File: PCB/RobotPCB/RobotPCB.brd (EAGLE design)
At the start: 50.8 x 50.8 mm, 42 parts, among them IC1 MPU6050, IC2 MCP73831/OT, U1 DRV8835, U2 CP2104-F03-GM

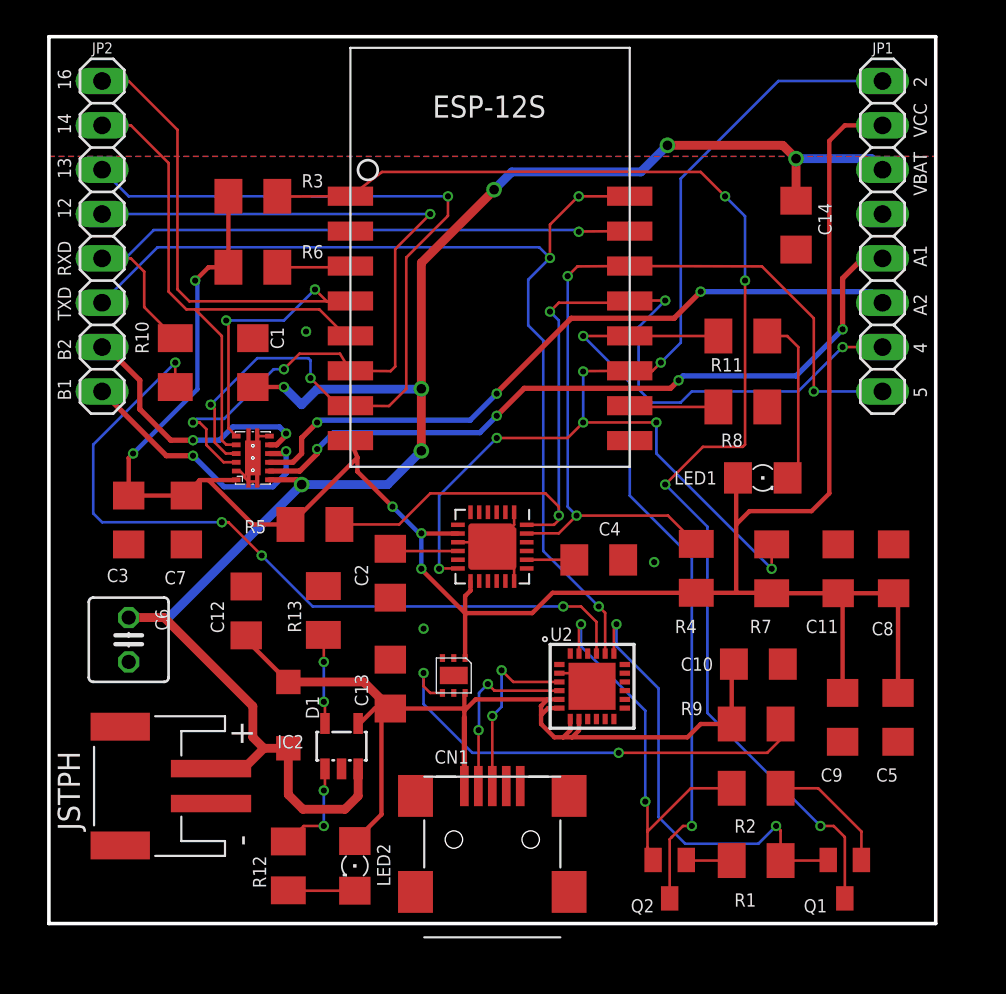
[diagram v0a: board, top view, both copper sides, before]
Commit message: Started some mounting holes
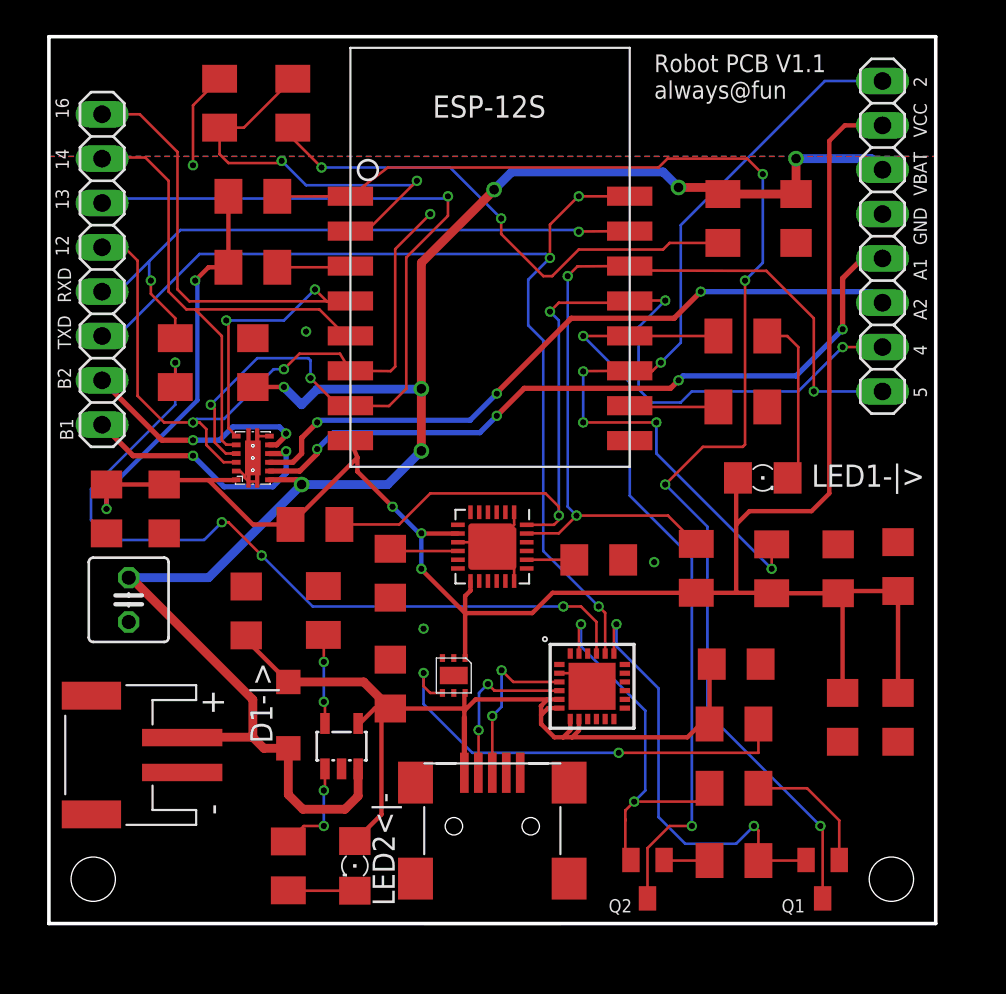
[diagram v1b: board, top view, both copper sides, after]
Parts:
- added R14: 10k, rcl:M1206
- added R15: 3.3k, rcl:M1206
- added R16: 1k, rcl:M1206
- R1: value 10ki -> 10k
- moved JSTPH 2.43 mm to (3.94, 9.65)
- moved C6 2.29 mm to (4.57, 18.5)
- moved JP2 1.90 mm to (3.05, 37.5)
- moved C3 1.42 mm to (3.30, 23.7)
- moved C7 1.42 mm to (6.60, 23.7)
- moved C10 1.27 mm to (39.4, 14.9)
- moved Q1 1.27 mm to (44.3, 2.54)
- moved Q2 1.27 mm to (34.3, 2.54)
- moved R1 1.27 mm to (39.2, 3.61)
- moved R2 1.27 mm to (39.2, 7.75)
- moved R9 1.27 mm to (39.2, 11.4)
- moved CN1 0.76 mm to (25.4, 4.57)
- moved C14 0.38 mm to (42.8, 40.4)
- moved C8 0.28 mm to (48.6, 20.4)
- renumbered D1 to D1-|>, LED1 to LED1-|>, LED2 to LED2<|-
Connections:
- new net N$6: R14.2, R16.1
- net ADC: now also R14.1, R15.2
- net GND: now also R15.1
- net GPIO2: no longer IC1.12
- net VBAT: now also R16.2
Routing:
- net N$6: track 0.00 -> 29.8 mm, vias 0 -> 2
- net ADC: track 0.00 -> 24.1 mm, vias 0 -> 2
- net GPIO2: track 64.4 -> 47.6 mm, vias 7 -> 5
- net GND: track 11.5 -> 17.1 mm, vias 3 -> 4
- net GPIO12: track 46.2 -> 41.3 mm
- net VCC: track 130.3 -> 134.3 mm
- net RESET: track 75.3 -> 77.8 mm
- net VBUS: track 56.4 -> 54.3 mm
- net MOUTB2: track 15.5 -> 13.7 mm
- net GPIO16: track 38.4 -> 36.9 mm
- net RXD: track 38.2 -> 36.8 mm, vias 1 -> 2
- net GPIO14: track 32.6 -> 31.3 mm
- net RTS: track 26.4 -> 25.1 mm
- net USB_RX: track 45.2 -> 46.4 mm
- net GPIO0: track 44.1 -> 45.1 mm
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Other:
- board text added: "GND"
- board text added: "Robot PCB V1.1 always@fun"

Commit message: Optimized Robot PCB
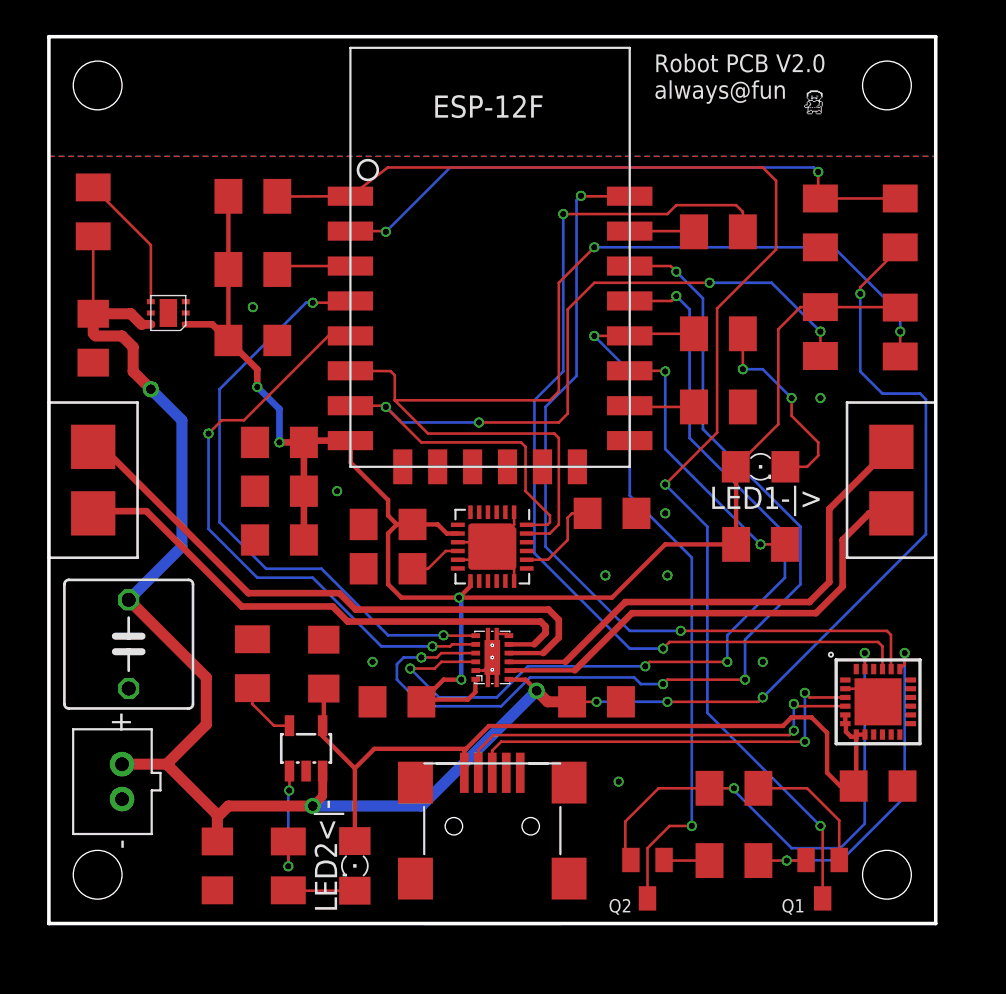
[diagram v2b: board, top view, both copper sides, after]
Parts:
- removed C6: 1.0 uF, rcl:C025-050X050
- removed D1-|>: MBR120HW, diode:SOD123
- removed JP1, JP2: (no value), pinhead:1X08
- removed JSTPH: (no value), adafruit:JST-PH-2-SMT-RA
- removed R16: 1k, rcl:M1206
- added C15: 1 mF, rcl:C050-075X075
- added CN2: (no value), adafruit:JST-PH-2-THM
- added U$3, U$4: MOTOR_PAD, ECE5780-MotorDriver:MOTOR_PAD
- R14: value 10k -> 39k
- R15: value 3.3k -> 10k
- moved C14 49.7 mm to (9.65, 3.30)
- moved R9 47.0 mm to (2.54, 40.8), turned to 90 degrees
- moved C10 41.3 mm to (2.54, 33.5), turned to 270 degrees
- moved C12 37.6 mm to (47.5, 7.87), turned to 0 degrees
- moved C5 36.9 mm to (13.2, 22.0), turned to 180 degrees
- moved C8 36.1 mm to (13.2, 27.6), turned to 180 degrees
- moved C11 36.0 mm to (11.7, 33.4), turned to 0 degrees
- moved R14 35.5 mm to (48.8, 40.1)
- moved R15 35.1 mm to (44.2, 40.1), turned to 90 degrees
- moved C9 34.8 mm to (13.2, 24.8), turned to 180 degrees
- moved R10 32.0 mm to (38.4, 39.6), turned to 180 degrees
- moved R5 31.0 mm to (44.2, 33.9), turned to 90 degrees
- moved C1 27.7 mm to (31.4, 12.7), turned to 0 degrees
- moved U$2 25.2 mm to (7.84, 36.0), turned to 180 degrees
- moved C3 20.0 mm to (19.9, 12.7), turned to 180 degrees
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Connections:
- removed net N$6: R14.2, R16.1
- net GND: now also C15.2, CN2.2; no longer C6.2, JP1.5, JSTPH.2
- net GPIO12: now also IC1.23, R4.1; no longer JP2.4, U1.10
- net GPIO13: now also IC1.24, R5.1; no longer JP2.3, U1.9
- net GPIO14: no longer JP2.2
- net GPIO16: no longer JP2.1
- net GPIO2: no longer JP1.8
- net GPIO4: now also U1.10; no longer IC1.24, JP1.2, R5.1
- net GPIO5: now also U1.9; no longer IC1.23, JP1.1, R4.1
- net MOUTA1: now also U$3.1; no longer JP1.4
- net MOUTA2: now also U$3.2; no longer JP1.3
- net MOUTB1: now also U$4.1; no longer JP2.8
- net MOUTB2: now also U$4.2; no longer JP2.7
- net RXD: no longer JP2.5
- net TXD: no longer JP2.6
- net VBAT: now also C10.1, C15.1, CN2.1, R14.2, R9.1, U$2.6; no longer C6.1, D1-|>.A, JP1.6, JSTPH.1, R16.2
- net VBUS: no longer C10.1, D1-|>.C, R9.1, U$2.6
- net VCC: no longer JP1.7
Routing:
- net VCC: track 134.3 -> 96.3 mm, vias 5 -> 4
- net RXD: track 36.8 -> 3.70 mm, vias 2 -> 0
- net GPIO2: track 47.6 -> 15.6 mm, vias 5 -> 2
- net N$6: track 29.8 -> 0.00 mm, vias 2 -> 0
- net MOUTB1: track 14.6 -> 35.0 mm, vias 2 -> 0
- net GPIO12: track 41.3 -> 61.6 mm, vias 3 -> 2
- net VBAT: track 101.9 -> 121.2 mm
- net N$3: track 25.8 -> 7.91 mm, vias 2 -> 0
- net MOUTB2: track 13.7 -> 31.4 mm, vias 2 -> 0
- net N$4: track 9.67 -> 24.6 mm
- net MOUTA1: track 42.0 -> 27.2 mm, vias 4 -> 0
- net N$7: track 9.56 -> 24.3 mm
- net TXD: track 59.8 -> 47.6 mm, vias 3 -> 2
- net MOUTA2: track 40.0 -> 29.5 mm, vias 3 -> 0
- net ADC: track 24.1 -> 34.6 mm
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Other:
- board text added: "Robot PCB V2.0 always@fun"
- board text removed: "12"
- board text removed: "13"
- board text removed: "14"
- board text removed: "16"
- board text removed: "2"
- board text removed: "4"
- board text removed: "5"
- board text removed: "A1"
- board text removed: "A2"
- board text removed: "B1"
- board text removed: "B2"
- board text removed: "GND"
- board text removed: "RXD"
- board text removed: "Robot PCB V1.1 always@fun"
- board text removed: "TXD"
- board text removed: "VBAT"
- board text removed: "VCC"

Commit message: Fixed PCB mounting holes
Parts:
- R14: value 39k -> 33k
- moved Q1 0.76 mm to (43.6, 2.54)
- moved Q2 0.76 mm to (33.5, 2.54)
- moved R1 0.76 mm to (38.5, 3.61)
- moved R2 0.76 mm to (38.5, 7.75)
- moved CN2 0.36 mm to (4.45, 8.38), turned to 0 degrees
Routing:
- net GPIO0: track 42.1 -> 43.0 mm
- net RTS: track 20.3 -> 21.1 mm
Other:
- board text added: "Robot PCB V2.1 always@fun"
- board text removed: "Robot PCB V2.0 always@fun"

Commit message: Finalized Robot PCB
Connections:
- net GND: now also U1.PAD5, U1.PAD6, U1.PAD7
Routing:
- net GND: track 15.6 -> 17.1 mm
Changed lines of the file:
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@@
 <contactref element="CN2" pad="2"/>
 <contactref element="C15" pad="2"/>
+<contactref element="U1" pad="PAD5"/>
+<contactref element="U1" pad="PAD6"/>
+<contactref element="U1" pad="PAD7"/>
+<wire x1="25.15" y1="13.89" x2="25.15" y2="14.244" width="0.1524" layer="1"/>
+<wire x1="25.15" y1="14.244" x2="24.904" y2="14.49" width="0.1524" layer="1"/>
+<wire x1="25.65" y1="13.89" x2="25.65" y2="14.355" width="0.1524" layer="1"/>
+<wire x1="25.65" y1="14.355" x2="25.4" y2="14.605" width="0.1524" layer="1"/>
 </signal>
 <signal name="VCC">
@@
 <contactref element="U1" pad="4"/>
 <contactref element="U$4" pad="1"/>
-<wire x1="26.35" y1="15.49" x2="28.317" y2="15.49" width="0.254" layer="1"/>
-<wire x1="28.317" y1="15.49" x2="29.21" y2="16.383" width="0.381" layer="1"/>
+<wire x1="29.21" y1="16.383" x2="28.317" y2="15.49" width="0.381" layer="1"/>
 <wire x1="29.21" y1="16.383" x2="29.21" y2="17.399" width="0.381" layer="1"/>
 <wire x1="29.21" y1="17.399" x2="28.6258" y2="17.9832" width="0.381" layer="1"/>
@@
 <wire x1="3.048" y1="27.305" x2="2.54" y2="27.305" width="0.381" layer="1"/>
 <wire x1="17.5768" y1="17.9832" x2="16.637" y2="18.923" width="0.381" layer="1"/>
+<wire x1="28.317" y1="15.49" x2="26.35" y2="15.49" width="0.254" layer="1"/>
 </signal>
 <signal name="MOUTB2">
